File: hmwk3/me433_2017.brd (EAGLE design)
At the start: 50 x 50 mm, 22 parts, among them J3 USB

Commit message: added pieces into board
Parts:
- moved C1 78.8 mm to (45.7, 27.9), turned to 90 degrees
- moved LED1 72.6 mm to (40.6, 44.5), turned to 180 degrees
- moved J3 66.6 mm to (44.5, 8.89), turned to 270 degrees
- moved U$5 64.5 mm to (16.5, 44.5), turned to 90 degrees
- moved C2 63.9 mm to (20.3, 3.81)
- moved C3 63.9 mm to (14.0, 3.81)
- moved C7 63.9 mm to (7.62, 3.81)
- moved U$2 59.2 mm to (30.5, 2.54)
- moved J1 57.6 mm to (2.54, 34.3)
- moved R4 52.4 mm to (6.35, 30.5)
- moved U$3 51.2 mm to (10.2, 12.7), turned to 90 degrees
- moved LED2 43.8 mm to (16.5, 27.9), turned to 180 degrees
- moved U$4 41.8 mm to (5.08, 19.1), turned to 90 degrees
- moved R3 38.1 mm to (6.35, 43.2)
- moved J2 37.0 mm to (2.54, 39.4)
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
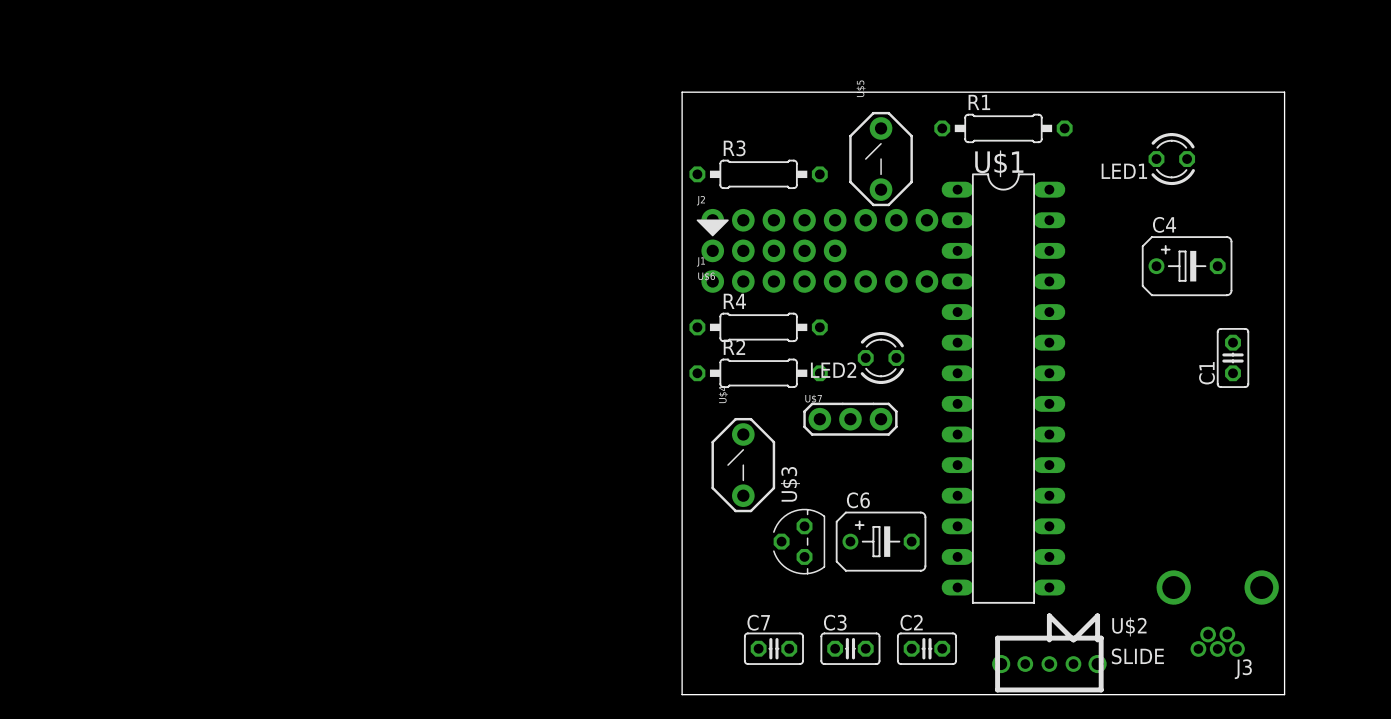
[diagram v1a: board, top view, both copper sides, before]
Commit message: still moving things around so the wires on the pic32 don't cross as much
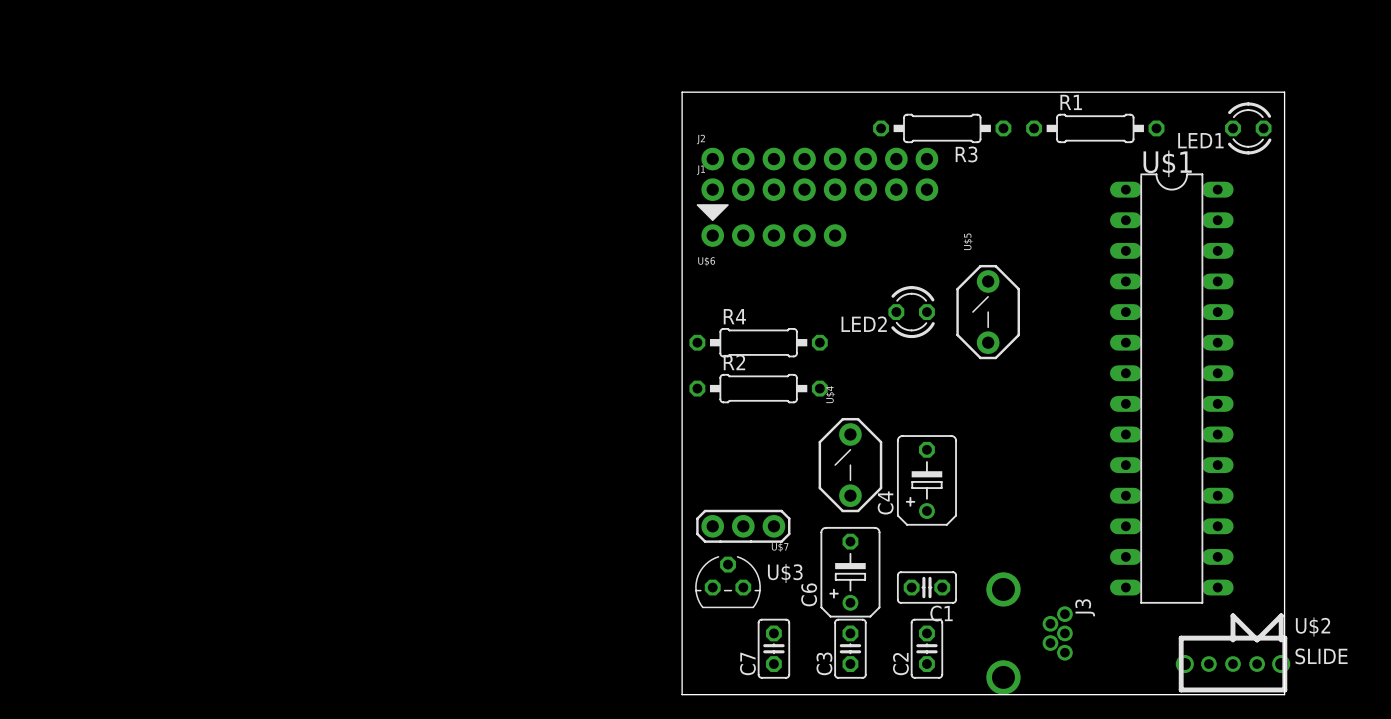
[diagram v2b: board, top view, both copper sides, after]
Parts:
- moved C1 31.8 mm to (20.3, 8.89), turned to 180 degrees
- moved C4 28.0 mm to (20.3, 17.8), turned to 90 degrees
- moved J3 18.2 mm to (26.7, 5.08), turned to 0 degrees
- moved R3 15.7 mm to (21.6, 47.0), turned to 180 degrees
- moved U$5 15.5 mm to (25.4, 31.8)
- moved U$2 15.2 mm to (45.7, 2.54)
- moved U$1 14.0 mm to (40.6, 25.4)
- moved U$7 12.6 mm to (5.08, 14.0), turned to 180 degrees
- moved U$4 8.89 mm to (14.0, 19.1)
- moved J1 7.62 mm to (2.54, 41.9)
- moved R1 7.62 mm to (34.3, 47.0)
- moved U$3 7.41 mm to (3.81, 8.89), turned to 0 degrees
- moved LED1 6.84 mm to (47.0, 47.0)
- moved J2 5.08 mm to (2.54, 44.5)
- moved LED2 4.58 mm to (19.1, 31.8)
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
